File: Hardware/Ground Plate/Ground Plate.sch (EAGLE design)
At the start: 9 parts

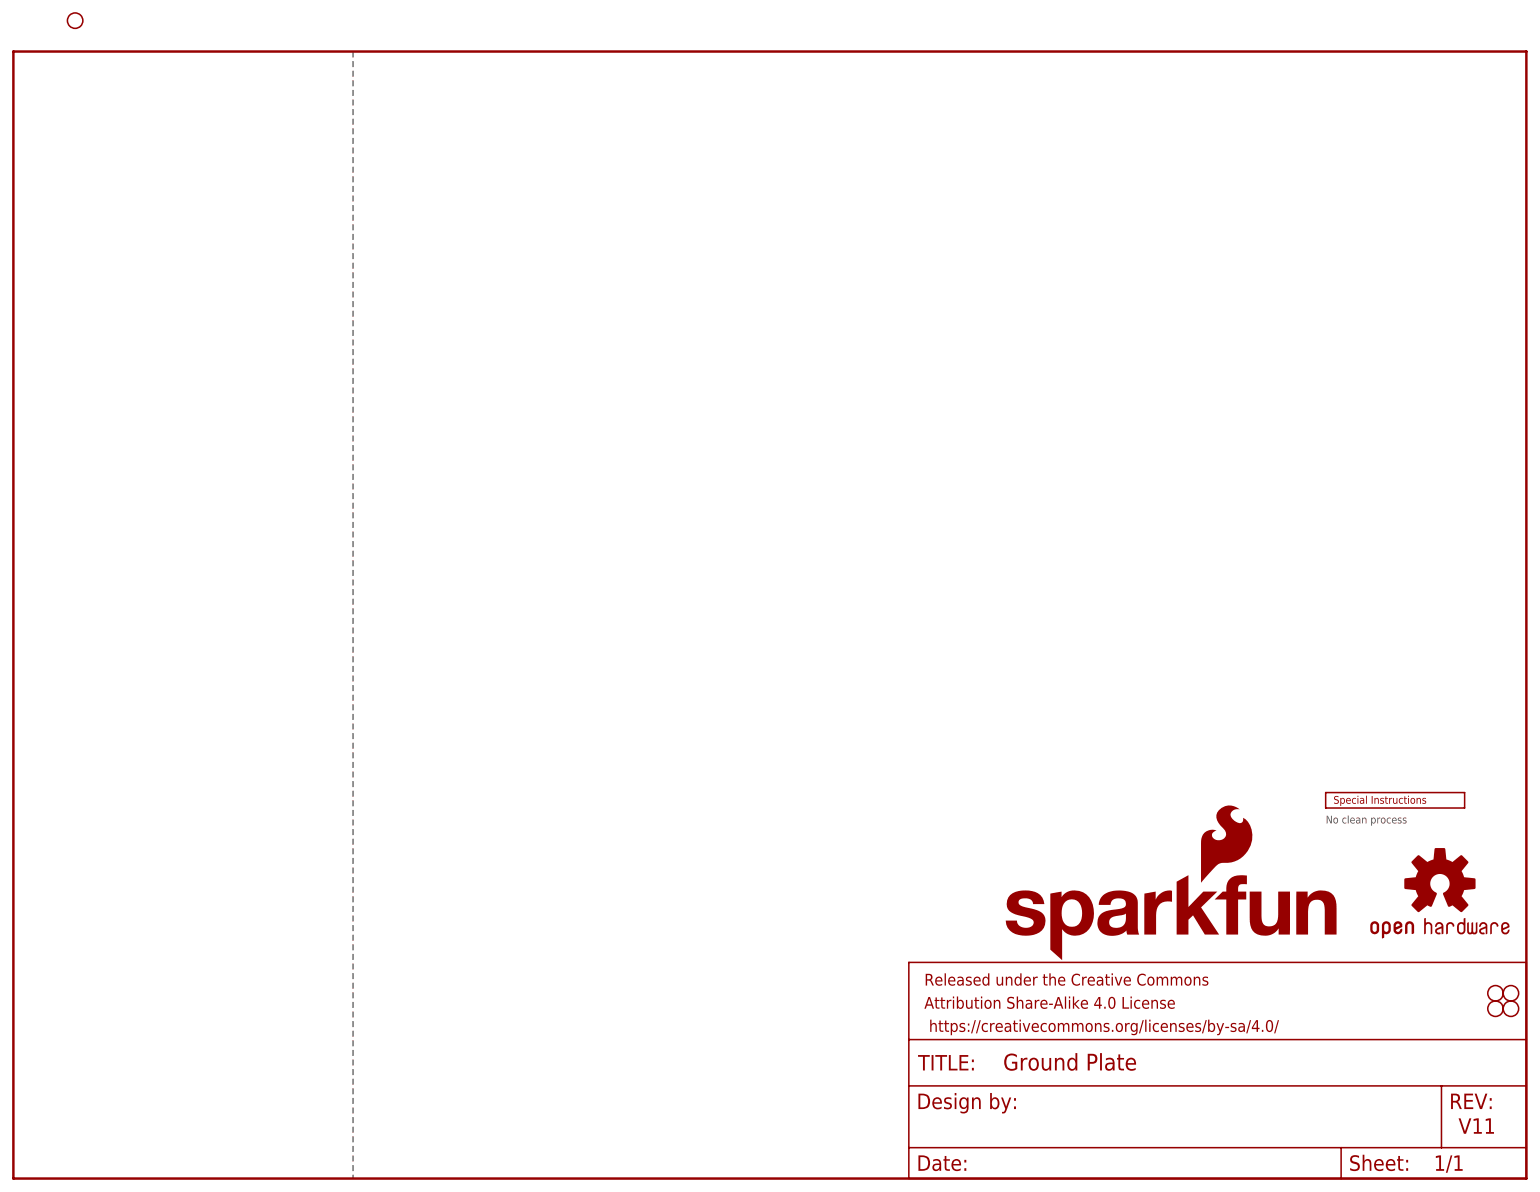
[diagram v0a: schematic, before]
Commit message: Combining ground plate versions
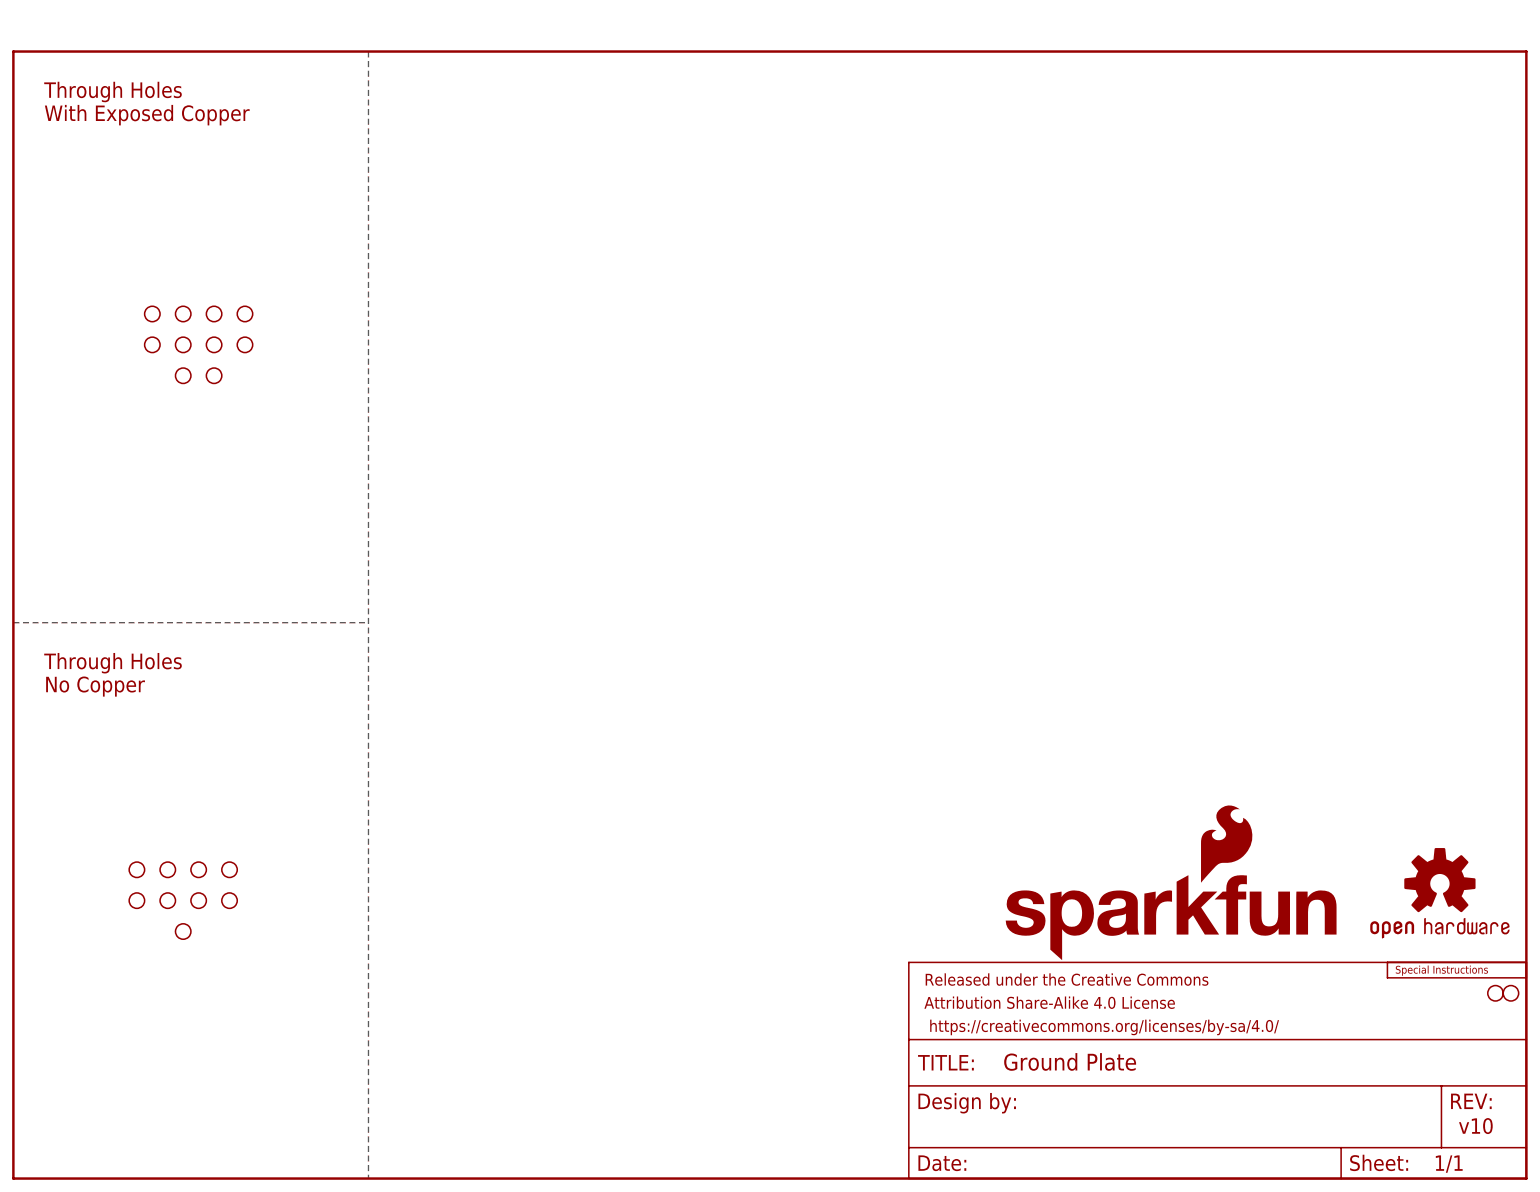
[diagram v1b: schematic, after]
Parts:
- removed JP101, JP41: STAND-OFF, SparkFun:STAND-OFF
- added U$10, U$11, U$12, U$22, U$5, U$6, U$7, U$8, U$9: SMA-ANTENNA-THREADED-NOT-KEYED_WITH-STOP, SparkFun-Hardware:SMA-ANTENNA-THREADED-NOT-KEYED_WITH-STOP
- added U$13, U$14, U$15, U$16, U$17, U$18, U$19, U$20, U$21: SMA-ANTENNA-THREADED-NOT-KEYED_NO-COPPER, SparkFun-Hardware:SMA-ANTENNA-THREADED-NOT-KEYED_NO-COPPER
- LOGO1: value OSHW-LOGOMINI -> OSHW-LOGOM; device SparkFun-Aesthetics:OSHW-LOGOMINI -> SparkFun-Aesthetics:OSHW-LOGOM
- LOGO2: value SFE_LOGO_NAME_FLAME.1_INCH -> SFE_LOGO_NAME_FLAME.5_INCH; device SparkFun-Aesthetics:SFE_LOGO_NAME_FLAME.1_INCH -> SparkFun-Aesthetics:SFE_LOGO_NAME_FLAME.5_INCH
- U$54: value SMA-ANTENNA-THREADED -> SMA-ANTENNA-THREADED-NOT-KEYED_WITH-STOP; device SparkFun-Hardware:SMA-ANTENNA-THREADED -> SparkFun-Hardware:SMA-ANTENNA-THREADED-NOT-KEYED_WITH-STOP
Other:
- note added: "Through Holes No Copper"
- note added: "Through Holes With Exposed Copper"
- note added: "v10"
- note removed: "No clean process"
- note removed: "V11"
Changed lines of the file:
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@@
 <drawing>
 <settings>
-<setting alwaysvectorfont="yes"/>
+<setting alwaysvectorfont="no"/>
 <setting keepoldvectorfont="yes"/>
 <setting verticaltext="up"/>
 </settings>
-<grid distance="0.1" unitdist="inch" unit="inch" style="lines" multiple="1" display="no" altdistance="0.01" altunitdist="inch" altunit="inch"/>
+<grid distance="0.1" unitdist="inch" unit="inch" style="lines" multiple="1" display="no" altdistance="0.05" altunitdist="inch" altunit="inch"/>
 <layers>
 <layer number="1" name="Top" color="4" fill="1" visible="no" active="no"/>
@@
 <layer number="56" name="wert" color="7" fill="1" visible="no" active="no"/>
 <layer number="57" name="tCAD" color="7" fill="1" visible="no" active="no"/>
+<layer number="58" name="bCAD" color="7" fill="1" visible="no" active="no"/>
 <layer number="59" name="tCarbon" color="7" fill="1" visible="no" active="no"/>
 <layer number="60" name="bCarbon" color="7" fill="1" visible="no" active="no"/>
@@
 <parts>
 <part name="JP31" library="SparkFun" deviceset="STAND-OFF" device=""/>
-<part name="JP41" library="SparkFun" deviceset="STAND-OFF" device=""/>
 <part name="FRAME1" library="SparkFun-Aesthetics" deviceset="FRAME-LETTER" device=""/>
-<part name="LOGO1" library="SparkFun-Aesthetics" deviceset="OSHW-LOGO" device="MINI"/>
+<part name="LOGO1" library="SparkFun-Aesthetics" deviceset="OSHW-LOGO" device="M" value="OSHW-LOGOM"/>
 <part name="JP91" library="SparkFun" deviceset="STAND-OFF" device=""/>
-<part name="JP101" library="SparkFun" deviceset="STAND-OFF" device=""/>
-<part name="LOGO2" library="SparkFun-Aesthetics" deviceset="SFE_LOGO_NAME_FLAME" device=".1_INCH"/>
+<part name="LOGO2" library="SparkFun-Aesthetics" deviceset="SFE_LOGO_NAME_FLAME" device=".5_INCH" value="SFE_LOGO_NAME_FLAME.5_INCH"/>
 <part name="U$2" library="SparkFun-Aesthetics" deviceset="SPECIAL_INSTRUCTIONS" device="-ORDERING"/>
-<part name="U$54" library="SparkFun-Hardware" deviceset="SMA-ANTENNA-THREADED" device=""/>
+<part name="U$54" library="SparkFun-Hardware" deviceset="SMA-ANTENNA-THREADED" device="-NOT-KEYED_WITH-STOP"/>
+<part name="U$5" library="SparkFun-Hardware" deviceset="SMA-ANTENNA-THREADED" device="-NOT-KEYED_WITH-STOP"/>
+<part name="U$6" library="SparkFun-Hardware" deviceset="SMA-ANTENNA-THREADED" device="-NOT-KEYED_WITH-STOP"/>
+<part name="U$7" library="SparkFun-Hardware" deviceset="SMA-ANTENNA-THREADED" device="-NOT-KEYED_WITH-STOP"/>
+<part name="U$8" library="SparkFun-Hardware" deviceset="SMA-ANTENNA-THREADED" device="-NOT-KEYED_WITH-STOP"/>
+<part name="U$9" library="SparkFun-Hardware" deviceset="SMA-ANTENNA-THREADED" device="-NOT-KEYED_WITH-STOP"/>
+<part name="U$10" library="SparkFun-Hardware" deviceset="SMA-ANTENNA-THREADED" device="-NOT-KEYED_WITH-STOP"/>
+<part name="U$11" library="SparkFun-Hardware" deviceset="SMA-ANTENNA-THREADED" device="-NOT-KEYED_WITH-STOP"/>
+<part name="U$12" library="SparkFun-Hardware" deviceset="SMA-ANTENNA-THREADED" device="-NOT-KEYED_WITH-STOP"/>
+<part name="U$13" library="SparkFun-Hardware" deviceset="SMA-ANTENNA-THREADED" device="-NOT-KEYED_NO-COPPER"/>
+<part name="U$14" library="SparkFun-Hardware" deviceset="SMA-ANTENNA-THREADED" device="-NOT-KEYED_NO-COPPER"/>
+<part name="U$15" library="SparkFun-Hardware" deviceset="SMA-ANTENNA-THREADED" device="-NOT-KEYED_NO-COPPER"/>
+<part name="U$16" library="SparkFun-Hardware" deviceset="SMA-ANTENNA-THREADED" device="-NOT-KEYED_NO-COPPER"/>
+<part name="U$17" library="SparkFun-Hardware" deviceset="SMA-ANTENNA-THREADED" device="-NOT-KEYED_NO-COPPER"/>
+<part name="U$18" library="SparkFun-Hardware" deviceset="SMA-ANTENNA-THREADED" device="-NOT-KEYED_NO-COPPER"/>
+<part name="U$19" library="SparkFun-Hardware" deviceset="SMA-ANTENNA-THREADED" device="-NOT-KEYED_NO-COPPER"/>
+<part name="U$20" library="SparkFun-Hardware" deviceset="SMA-ANTENNA-THREADED" device="-NOT-KEYED_NO-COPPER"/>
+<part name="U$21" library="SparkFun-Hardware" deviceset="SMA-ANTENNA-THREADED" device="-NOT-KEYED_NO-COPPER"/>
+<part name="U$22" library="SparkFun-Hardware" deviceset="SMA-ANTENNA-THREADED" device="-NOT-KEYED_WITH-STOP"/>
 </parts>
 <sheets>
 <sheet>
 <plain>
-<text x="237.744" y="7.366" size="2.54" layer="94">V11</text>
-<wire x1="55.88" y1="185.42" x2="55.88" y2="0" width="0.1524" layer="97" style="longdash"/>
-<text x="215.9" y="58.42" size="1.27" layer="97">No clean process</text>
+<text x="237.744" y="7.366" size="2.54" layer="94">v10</text>
+<wire x1="58.42" y1="185.42" x2="58.42" y2="0" width="0.1524" layer="97" style="longdash"/>
+<text x="5.08" y="180.34" size="2.54" layer="94" font="vector" ratio="12" align="top-left">Through Holes
+With Exposed Copper</text>
+<wire x1="0" y1="91.44" x2="58.42" y2="91.44" width="0.1524" layer="97" style="longdash"/>
+<text x="5.08" y="86.36" size="2.54" layer="94" font="vector" ratio="12" align="top-left">Through Holes
+No Copper</text>
 </plain>
 <instances>
 <instance part="JP31" gate="G$1" x="246.38" y="30.48" smashed="yes"/>
-<instance part="JP41" gate="G$1" x="246.38" y="27.94" smashed="yes"/>
 <instance part="FRAME1" gate="G$1" x="0" y="0" smashed="yes"/>
 <instance part="FRAME1" gate="V" x="147.32" y="0" smashed="yes">
@@
 <instance part="LOGO1" gate="G$1" x="234.696" y="48.514" smashed="yes"/>
 <instance part="JP91" gate="G$1" x="243.84" y="30.48" smashed="yes"/>
-<instance part="JP101" gate="G$1" x="243.84" y="27.94" smashed="yes"/>
 <instance part="LOGO2" gate="G$1" x="162.56" y="35.56" smashed="yes"/>
-<instance part="U$2" gate="G$1" x="215.9" y="60.96" smashed="yes"/>
-<instance part="U$54" gate="G$1" x="10.16" y="190.5" smashed="yes"/>
+<instance part="U$2" gate="G$1" x="226.06" y="33.02" smashed="yes"/>
+<instance part="U$54" gate="G$1" x="22.86" y="137.16" smashed="yes"/>
+<instance part="U$5" gate="G$1" x="22.86" y="142.24" smashed="yes"/>
+<instance part="U$6" gate="G$1" x="27.94" y="137.16" smashed="yes"/>
+<instance part="U$7" gate="G$1" x="27.94" y="142.24" smashed="yes"/>
+<instance part="U$8" gate="G$1" x="33.02" y="142.24" smashed="yes"/>
+<instance part="U$9" gate="G$1" x="33.02" y="137.16" smashed="yes"/>
+<instance part="U$10" gate="G$1" x="38.1" y="142.24" smashed="yes"/>
+<instance part="U$11" gate="G$1" x="38.1" y="137.16" smashed="yes"/>
+<instance part="U$12" gate="G$1" x="27.94" y="132.08" smashed="yes"/>
+<instance part="U$13" gate="G$1" x="20.32" y="50.8" smashed="yes"/>
+<instance part="U$14" gate="G$1" x="25.4" y="50.8" smashed="yes"/>
+<instance part="U$15" gate="G$1" x="30.48" y="50.8" smashed="yes"/>
+<instance part="U$16" gate="G$1" x="35.56" y="50.8" smashed="yes"/>
+<instance part="U$17" gate="G$1" x="20.32" y="45.72" smashed="yes"/>
+<instance part="U$18" gate="G$1" x="25.4" y="45.72" smashed="yes"/>
+<instance part="U$19" gate="G$1" x="30.48" y="45.72" smashed="yes"/>
+<instance part="U$20" gate="G$1" x="35.56" y="45.72" smashed="yes"/>
+<instance part="U$21" gate="G$1" x="27.94" y="40.64" smashed="yes"/>
+<instance part="U$22" gate="G$1" x="33.02" y="132.08" smashed="yes"/>
 </instances>
 <busses>
